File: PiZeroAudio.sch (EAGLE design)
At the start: 63 parts, among them CON1 RPI-ZERO, J1 2X1-LOCKING, J2 4X1-LOCKING, Q1 DMG2305UX, U1 TXB0104PWR, U2 LSM6DS33, U3 NC7WZ16, U4 DMMT5401, U5 TPA3144D2PWPR

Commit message: PostGrove
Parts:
- removed JP2: GPIO, adafruit:PINHD-2X4
- added J3: GROVE, HappyBrackets:GROVE
- added J4: 2X2HEADER, HappyBrackets:2X2HEADER
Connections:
- removed net N$11: JP2.1, U1.B1
- removed net N$12: JP2.3, U1.B2
- removed net N$14: JP2.5, U1.B3
- removed net N$15: JP2.7, U1.B4
- new net GPI022-OUT: J4.1, U1.B3
- new net GPIO21-OUT: J4.3, U1.B4
- new net GPIO23-OUT: J3.1, U1.B2
- new net GPIO25-OUT: J3.2, U1.B1
- net +5V: now also J3.3
- net GND: now also J3.4, J4.2, J4.4; no longer JP2.2, JP2.4, JP2.6, JP2.8
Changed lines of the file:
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@@
 <part name="R18" library="adafruit" deviceset="R-US_" device="R0603" value="33K"/>
 <part name="+3V35" library="supply1" library_urn="urn:adsk.eagle:library:371" deviceset="+3V3" device=""/>
-<part name="JP2" library="adafruit" deviceset="PINHD-2X4" device="" value="GPIO"/>
 <part name="SUPPLY4" library="supply2" library_urn="urn:adsk.eagle:library:372" deviceset="GND" device=""/>
 <part name="SUPPLY7" library="supply2" library_urn="urn:adsk.eagle:library:372" deviceset="GND" device=""/>
@@
 <part name="R13" library="adafruit" deviceset="R-US_" device="R0603" value="10K"/>
 <part name="AGND9" library="supply1" library_urn="urn:adsk.eagle:library:371" deviceset="AGND" device=""/>
+<part name="J3" library="HappyBrackets" library_urn="urn:adsk.eagle:library:5224691" deviceset="GROVE" device=""/>
+<part name="SUPPLY13" library="supply2" library_urn="urn:adsk.eagle:library:372" deviceset="GND" device=""/>
+<part name="J4" library="HappyBrackets" library_urn="urn:adsk.eagle:library:5224691" deviceset="2X2HEADER" device=""/>
+<part name="P+6" library="supply1" library_urn="urn:adsk.eagle:library:371" deviceset="+5V" device=""/>
 </parts>
 <sheets>
@@
 <instance part="R8" gate="G$1" x="-281.94" y="149.86" rot="R180"/>
 <instance part="R9" gate="G$1" x="-274.32" y="144.78" rot="R90"/>
-<instance part="P+2" gate="1" x="-327.66" y="195.58" smashed="yes" rot="R270">
-<attribute name="VALUE" x="-327.66" y="198.12" size="1.778" layer="96"/>
+<instance part="P+2" gate="1" x="-325.12" y="195.58" smashed="yes" rot="R270">
+<attribute name="VALUE" x="-322.58" y="195.58" size="1.778" layer="96"/>
 </instance>
 <instance part="U3" gate="G$1" x="-304.8" y="157.48"/>
@@
 <attribute name="VALUE" x="-394.716" y="178.816" size="1.778" layer="96" rot="R180"/>
 </instance>
-<instance part="JP2" gate="A" x="-248.92" y="215.9"/>
-<instance part="SUPPLY4" gate="GND" x="-243.84" y="205.74" smashed="yes"/>
+<instance part="SUPPLY4" gate="GND" x="-220.98" y="195.58" smashed="yes"/>
 <instance part="SUPPLY7" gate="GND" x="-335.28" y="172.72" smashed="yes"/>
 <instance part="SUPPLY6" gate="GND" x="-411.48" y="185.42" smashed="yes"/>
@@
 <instance part="R13" gate="G$1" x="-269.24" y="88.9" rot="R270"/>
 <instance part="AGND9" gate="VR1" x="-269.24" y="78.74"/>
+<instance part="J3" gate="G$1" x="-226.06" y="220.98" rot="MR180"/>
+<instance part="SUPPLY13" gate="GND" x="-231.14" y="228.6" smashed="yes" rot="R180"/>
+<instance part="J4" gate="G$1" x="-231.14" y="198.12"/>
+<instance part="P+6" gate="1" x="-241.3" y="223.52" smashed="yes" rot="R90">
+<attribute name="VALUE" x="-241.3" y="226.06" size="1.778" layer="96" rot="R180"/>
+</instance>
 </instances>
 <busses>
@@
 </segment>
 <segment>
-<pinref part="JP2" gate="A" pin="2"/>
-<wire x1="-243.84" y1="220.98" x2="-243.84" y2="218.44" width="0.1524" layer="91"/>
-<pinref part="SUPPLY4" gate="GND" pin="GND"/>
-<pinref part="JP2" gate="A" pin="4"/>
-<wire x1="-243.84" y1="218.44" x2="-243.84" y2="215.9" width="0.1524" layer="91"/>
-<junction x="-243.84" y="218.44"/>
-<pinref part="JP2" gate="A" pin="6"/>
-<wire x1="-243.84" y1="215.9" x2="-243.84" y2="213.36" width="0.1524" layer="91"/>
-<junction x="-243.84" y="215.9"/>
-<pinref part="JP2" gate="A" pin="8"/>
-<wire x1="-243.84" y1="213.36" x2="-243.84" y2="208.28" width="0.1524" layer="91"/>
-<junction x="-243.84" y="213.36"/>
-</segment>
-<segment>
 <pinref part="SUPPLY12" gate="GND" pin="GND"/>
 <pinref part="SH2" gate="G$1" pin="DIG"/>
@@
 <wire x1="-317.5" y1="213.36" x2="-317.5" y2="223.52" width="0.1524" layer="91"/>
 </segment>
+<segment>
+<pinref part="J3" gate="G$1" pin="4"/>
+<pinref part="SUPPLY13" gate="GND" pin="GND"/>
+</segment>
+<segment>
+<pinref part="J4" gate="G$1" pin="2"/>
+<pinref part="SUPPLY4" gate="GND" pin="GND"/>
+<wire x1="-220.98" y1="203.2" x2="-220.98" y2="200.66" width="0.1524" layer="91"/>
+<pinref part="J4" gate="G$1" pin="4"/>
+<wire x1="-220.98" y1="200.66" x2="-220.98" y2="198.12" width="0.1524" layer="91"/>
+<junction x="-220.98" y="200.66"/>
+</segment>
 </net>
 <net name="PWM-R" class="0">
@@
 <wire x1="-340.36" y1="195.58" x2="-335.28" y2="195.58" width="0.1524" layer="91"/>
 <pinref part="CON1" gate="G$1" pin="5V0@1"/>
-<wire x1="-335.28" y1="195.58" x2="-330.2" y2="195.58" width="0.1524" layer="91"/>
+<wire x1="-335.28" y1="195.58" x2="-327.66" y2="195.58" width="0.1524" layer="91"/>
 <wire x1="-340.36" y1="198.12" x2="-340.36" y2="195.58" width="0.1524" layer="91"/>
 <junction x="-340.36" y="195.58"/>
@@
 <wire x1="-269.24" y1="109.22" x2="-269.24" y2="119.38" width="0.1524" layer="91"/>
 <junction x="-269.24" y="119.38"/>
+</segment>
+<segment>
+<pinref part="J3" gate="G$1" pin="3"/>
+<pinref part="P+6" gate="1" pin="+5V"/>
+<wire x1="-238.76" y1="223.52" x2="-231.14" y2="223.52" width="0.1524" layer="91"/>
 </segment>
 </net>
@@
 </segment>
 </net>
-<net name="N$11" class="0">
+<net name="GPIO25-OUT" class="0">
 <segment>
 <pinref part="U1" gate="G$1" pin="B1"/>
-<pinref part="JP2" gate="A" pin="1"/>
 <wire x1="-264.16" y1="220.98" x2="-251.46" y2="220.98" width="0.1524" layer="91"/>
-</segment>
-</net>
-<net name="N$12" class="0">
+<pinref part="J3" gate="G$1" pin="2"/>
+<wire x1="-251.46" y1="220.98" x2="-231.14" y2="220.98" width="0.1524" layer="91"/>
+<label x="-261.62" y="220.98" size="1.778" layer="95"/>
+</segment>
+</net>
+<net name="GPIO23-OUT" class="0">
 <segment>
 <pinref part="U1" gate="G$1" pin="B2"/>
-<pinref part="JP2" gate="A" pin="3"/>
-<wire x1="-264.16" y1="218.44" x2="-251.46" y2="218.44" width="0.1524" layer="91"/>
-</segment>
-</net>
-<net name="N$14" class="0">
+<wire x1="-264.16" y1="218.44" x2="-246.38" y2="218.44" width="0.1524" layer="91"/>
+<pinref part="J3" gate="G$1" pin="1"/>
+<wire x1="-231.14" y1="218.44" x2="-246.38" y2="218.44" width="0.1524" layer="91"/>
+<label x="-261.62" y="218.44" size="1.778" layer="95"/>
+</segment>
+</net>
+<net name="GPI022-OUT" class="0">
 <segment>
 <pinref part="U1" gate="G$1" pin="B3"/>
-<pinref part="JP2" gate="A" pin="5"/>
 <wire x1="-264.16" y1="215.9" x2="-251.46" y2="215.9" width="0.1524" layer="91"/>
-</segment>
-</net>
-<net name="N$15" class="0">
+<pinref part="J4" gate="G$1" pin="1"/>
+<wire x1="-241.3" y1="203.2" x2="-248.92" y2="203.2" width="0.1524" layer="91"/>
+<wire x1="-248.92" y1="203.2" x2="-248.92" y2="215.9" width="0.1524" layer="91"/>
+<wire x1="-248.92" y1="215.9" x2="-251.46" y2="215.9" width="0.1524" layer="91"/>
+<label x="-261.62" y="215.9" size="1.778" layer="95"/>
+</segment>
+</net>
+<net name="GPIO21-OUT" class="0">
 <segment>
 <pinref part="U1" gate="G$1" pin="B4"/>
-<pinref part="JP2" gate="A" pin="7"/>
 <wire x1="-264.16" y1="213.36" x2="-251.46" y2="213.36" width="0.1524" layer="91"/>
-</segment>
-</net>
+<wire x1="-251.46" y1="213.36" x2="-251.46" y2="200.66" width="0.1524" layer="91"/>
+<pinref part="J4" gate="G$1" pin="3"/>
+<wire x1="-251.46" y1="200.66" x2="-241.3" y2="200.66" width="0.1524" layer="91"/>
+<label x="-261.62" y="213.36" size="1.778" layer="95"/>
+</segment>
+</net>

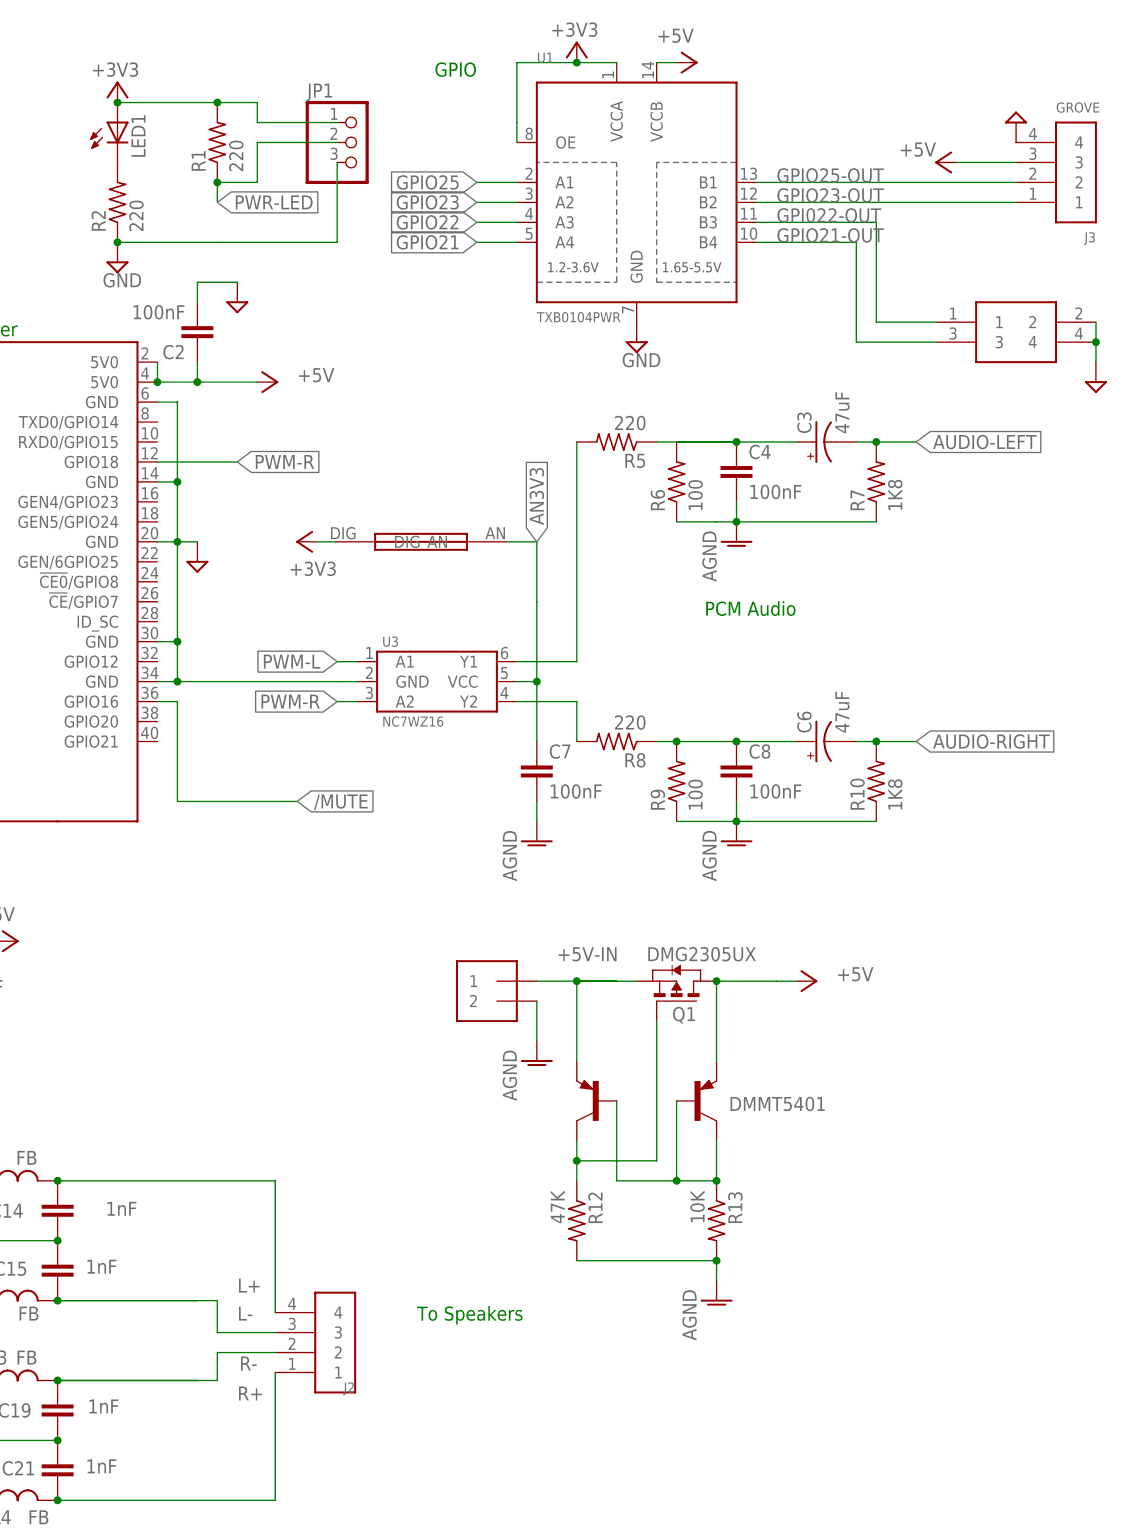
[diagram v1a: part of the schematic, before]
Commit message: Renumbered parts and aligned text
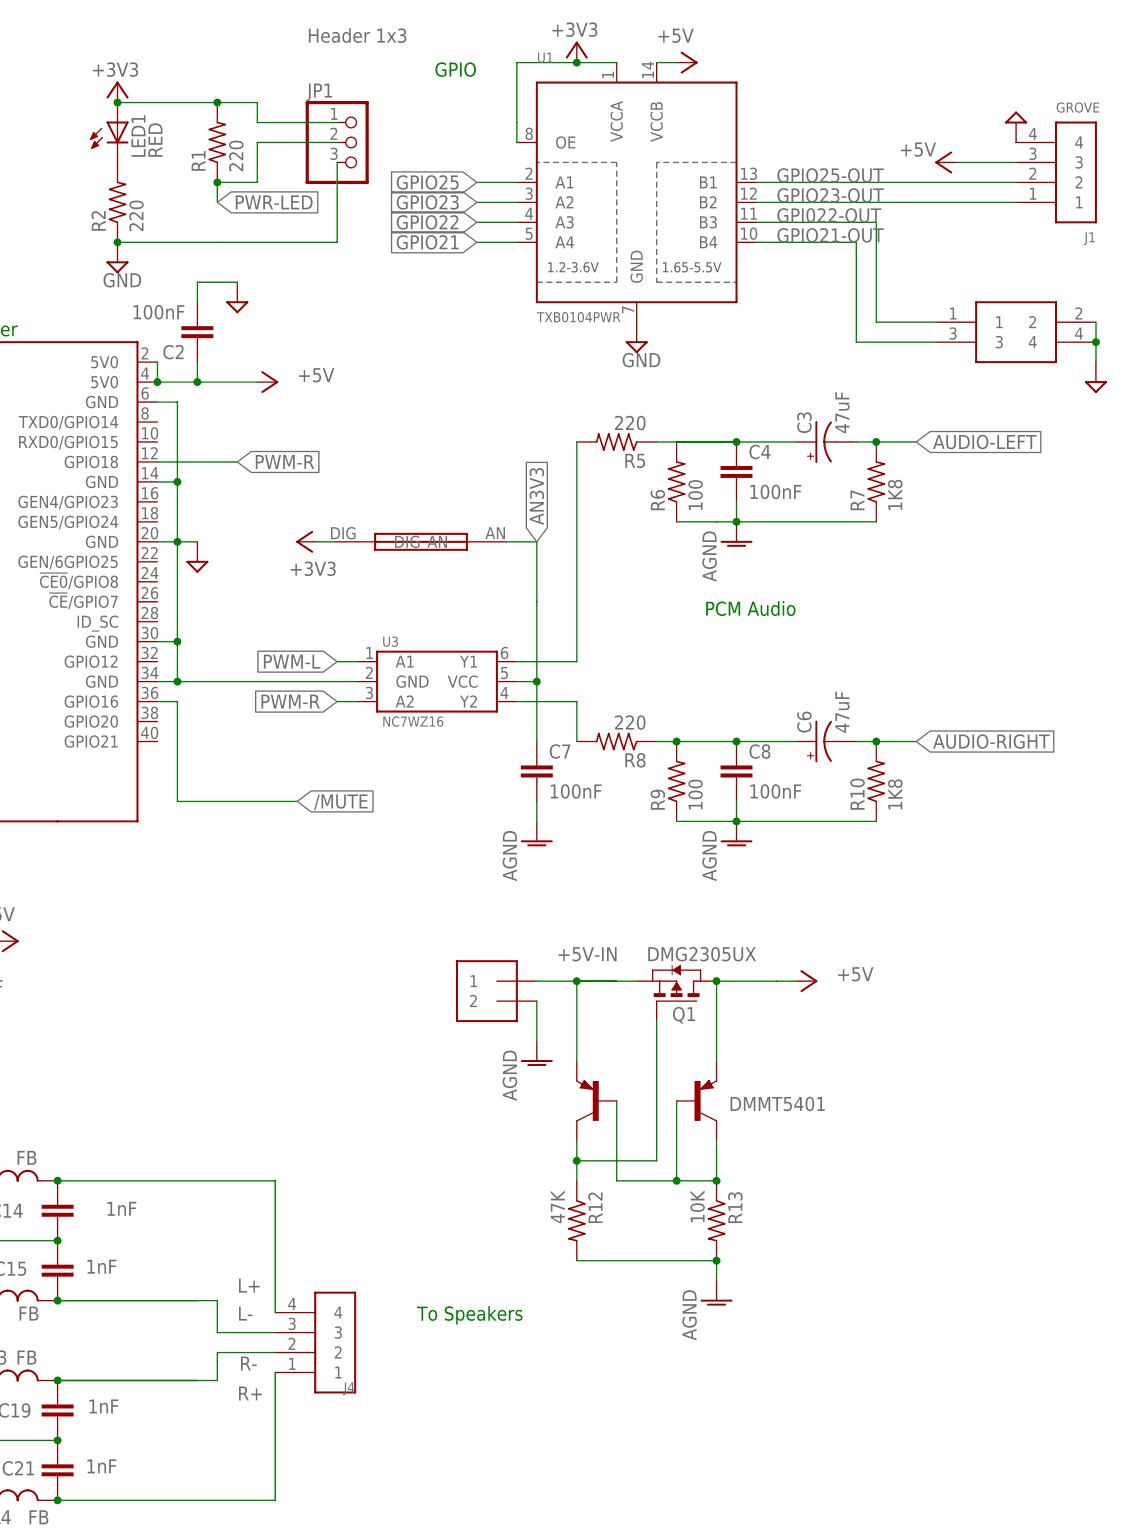
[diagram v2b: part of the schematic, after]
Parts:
- J1: value 2X1-LOCKING -> GROVE; device HappyBrackets:2X1-LOCKING -> HappyBrackets:GROVE
- J2: value 4X1-LOCKING -> 2X2HEADER; device HappyBrackets:4X1-LOCKING -> HappyBrackets:2X2HEADER
- J3: value GROVE -> 2X1-LOCKING; device HappyBrackets:GROVE -> HappyBrackets:2X1-LOCKING
- J4: value 2X2HEADER -> 4X1-LOCKING; device HappyBrackets:2X2HEADER -> HappyBrackets:4X1-LOCKING
- JP1: value (none) -> Header 1x3
- LED1: value (none) -> RED
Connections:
- net +5V: now also J1.3; no longer J3.3
- net +5V-IN: now also J3.1; no longer J1.1
- net AGND: now also J3.2; no longer J1.2
- net GND: now also J1.4, J2.2, J2.4; no longer J3.4, J4.2, J4.4
- net GPI022-OUT: now also J2.1; no longer J4.1
- net GPIO21-OUT: now also J2.3; no longer J4.3
- net GPIO23-OUT: now also J1.1; no longer J3.1
- net GPIO25-OUT: now also J1.2; no longer J3.2
- net L+: now also J4.4; no longer J2.4
- net L-: now also J4.3; no longer J2.3
- net R+: now also J4.1; no longer J2.1
- net R-: now also J4.2; no longer J2.2
